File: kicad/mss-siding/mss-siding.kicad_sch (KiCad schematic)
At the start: 154 parts

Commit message: Add relay part number
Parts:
- K? (x3): value Panasonic_AGQ -> AGQ200A4H
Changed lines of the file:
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@@
     (in_bom yes) (on_board yes) (fields_autoplaced)
     (property "Reference" "K?" (id 0) (at 307.34 26.67 90))
-    (property "Value" "Panasonic_AGQ" (id 1) (at 307.34 29.21 90))
+    (property "Value" "AGQ200A4H" (id 1) (at 307.34 29.21 90))
     (property "Footprint" "Relay_THT:Relay_DPDT_Kemet_EC2" (id 2) (at 287.02 45.72 0)
       (effects (font (size 1.27 1.27)) hide)
@@
     (in_bom yes) (on_board yes) (fields_autoplaced)
     (property "Reference" "K?" (id 0) (at 319.405 96.52 90))
-    (property "Value" "Panasonic_AGQ" (id 1) (at 319.405 99.06 90))
+    (property "Value" "AGQ200A4H" (id 1) (at 319.405 99.06 90))
     (property "Footprint" "Relay_THT:Relay_DPDT_Kemet_EC2" (id 2) (at 299.085 115.57 0)
       (effects (font (size 1.27 1.27)) hide)
@@
   (symbol (lib_id "ISE_Generic:Panasonic_AGQ") (at 319.405 80.645 270) (mirror x) (unit 1)
     (in_bom yes) (on_board yes) (fields_autoplaced)
-    (property "Reference" "K?" (id 0) (at 319.405 61.595 90))
-    (property "Value" "Panasonic_AGQ" (id 1) (at 319.405 64.135 90))
+    (property "Reference" "K?" (id 0) (at 319.405 60.96 90))
+    (property "Value" "AGQ200A4H" (id 1) (at 319.405 63.5 90))
     (property "Footprint" "Relay_THT:Relay_DPDT_Kemet_EC2" (id 2) (at 299.085 80.645 0)
       (effects (font (size 1.27 1.27)) hide)
@@
     )
     (path "/29be23f3-d869-4d7a-be2a-612e20353779"
-      (reference "K?") (unit 1) (value "Panasonic_AGQ") (footprint "Relay_THT:Relay_DPDT_Kemet_EC2")
+      (reference "K?") (unit 1) (value "AGQ200A4H") (footprint "Relay_THT:Relay_DPDT_Kemet_EC2")
     )
     (path "/97b96930-9823-47ee-a628-f48c3e51fdb3"
-      (reference "K?") (unit 1) (value "Panasonic_AGQ") (footprint "Relay_THT:Relay_DPDT_Kemet_EC2")
+      (reference "K?") (unit 1) (value "AGQ200A4H") (footprint "Relay_THT:Relay_DPDT_Kemet_EC2")
     )
     (path "/c24a1838-bf5f-4b70-8cd9-fe7905500def"
-      (reference "K?") (unit 1) (value "Panasonic_AGQ") (footprint "Relay_THT:Relay_DPDT_Kemet_EC2")
+      (reference "K?") (unit 1) (value "AGQ200A4H") (footprint "Relay_THT:Relay_DPDT_Kemet_EC2")
     )
     (path "/1d1dcbdd-9d00-47cf-8c81-961826a4a57a"

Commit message: First cut of PCB
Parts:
- removed R? (x8): 10k, Resistor_SMD:R_0805_2012Metric, symbol Device:R_US
- added C20: 10uF, Capacitor_SMD:C_0805_2012Metric, symbol Device:C
- added R30, R31, R32, R33, R34, R35, R36, R38: 10k, Resistor_SMD:R_0805_2012Metric, symbol Device:R_US
- added unit 3 of U3
- added unit 2 of U3
- added unit 1 of U4
- added unit 2 of U4
- JP14, JP15, JP5: renamed from JP?; footprint (none) -> Jumper:SolderJumper-2_P1.3mm_Bridged_RoundedPad1.0x1.5mm
- K1, K2, K3: renamed from K?; footprint Relay_THT:Relay_DPDT_Kemet_EC2 -> ISE_UltraLibrarian:RELAY_AGQ_A_PAN
- gave numbers to parts that had none: 128
- renumbered H3 to H2, H2 to H3
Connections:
- net +12V: now also R25.2; no longer R25.1
- net +5V: now also J19.3 (Pin_3), C20.1; no longer J19.1 (Pin_1)
- net A_L_SIGNAL_G: now also J18.4 (MOSI), U6.1 (PB0); no longer U6.4 (PB3)
- net A_L_SIGNAL_R: now also U6.14 (PA4); no longer U6.12 (PA6), U6.17 (AREF/PA3)
- net A_L_SIGNAL_Y: now also U6.17 (AREF/PA3); no longer U6.11 (PA7), U6.14 (PA4)
- net A_U_SIGNAL_R: now also U6.11 (PA7)
- net A_U_SIGNAL_Y: now also U6.12 (PA6)
- net B_SIGNAL_G: now also U6.7 (XTAL1/PB4); no longer J18.4 (MOSI), U6.1 (PB0)
- net B_SIGNAL_R: now also U6.9 (PB6); no longer J18.3 (SCK), U6.3 (PB2)
- net B_SIGNAL_Y: now also U6.8 (XTAL2/PB5); no longer J18.1 (MISO), U6.2 (PB1)
- net COM_SENSE: now also U5.4 (IO0_0); no longer U5.13 (IO1_0)
- net C_SIGNAL_G: now also J18.1 (MISO), U6.2 (PB1); no longer U6.9 (PB6)
- net C_SIGNAL_R: now also U6.4 (PB3); no longer U6.7 (XTAL1/PB4)
- net C_SIGNAL_Y: now also J18.3 (SCK), U6.3 (PB2); no longer U6.8 (XTAL2/PB5)
- net FORCE_POINTS_AA: now also U5.10 (IO0_6); no longer U5.14 (IO1_1)
- net GND: now also C1.2, D4.2 (A), D5.2 (A), J19.1 (Pin_1), K3.3, C20.2, U3.5, U3.7, U4.3, U4.5; no longer J1.MP (MountPin), J11.MP (MountPin), J12.MP (MountPin), J19.3 (Pin_3), J2.MP (MountPin), K3.6
- net MAIN_AA_IN: now also R27.2, R35.1
- net MAIN_A_OUT: now also K3.4, K3.7; no longer K3.2, K3.5
- net POINTS_AA_IN: now also R26.2, R34.1
- net POINTS_AA_OUT: now also R24.2, R32.1
- net POINTS_A_IN: now also R25.1, R33.1
- net POINTS_A_OUT: now also R23.2, R31.1
- net POINTS_S: now also K3.6, R22.2, R30.1; no longer K3.3
- net RELAY_DRV: now also U5.11 (IO0_7); no longer U5.15 (IO1_2)
- net SIDE_AA_IN: now also R28.2, R36.1
- net SIDE_A_OUT: now also K3.2, K3.5; no longer K3.4, K3.7
- net TO_NORMAL: now also R29.2, R38.1
- net at J1.4 (Pin_4), J11.4 (Pin_4), J12.4 (Pin_4)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: now also J1.MP (MountPin), J11.MP (MountPin), J12.MP (MountPin), J2.MP (MountPin)
- net OPTION_D: now reaches U5.8 (IO0_4)
- net OPTION_D: now also JP19.2 (B); no longer U4.2
- net OPTION_B: now reaches U5.6 (IO0_2)
- net OPTION_B: now also JP17.2 (B); no longer U4.2
- net at U5.17 (IO1_4): now also U3.12; no longer JP19.2 (B)
- net at U5.16 (IO1_3): now also U3.10; no longer JP20.2 (B)
- net at U3.2: now also U5.19 (IO1_6); no longer U5.11 (IO0_7)
- net at C15.1, U3.3: now also R38.2; no longer R29.2
- net at U5.20 (IO1_7): now also U4.6; no longer JP16.2 (B)
- net at U5.18 (IO1_5): now also U3.15; no longer JP18.2 (B)
- net OPTION_E: now reaches U5.9 (IO0_5)
- net OPTION_E: now also JP20.2 (B); no longer U4.2
- net OPTION_A: now reaches U5.5 (IO0_1)
- net OPTION_A: now also JP16.2 (B); no longer U3.2
- net OPTION_C: now reaches U5.7 (IO0_3)
- net OPTION_C: now also JP18.2 (B); no longer U3.2
- new net: C14.1, R35.2, U4.7
- new net: C18.1, R34.2, U4.14
- new net: U4.15, U5.15 (IO1_2)
- new net: C16.1, R30.2, U3.14
- new net: C17.1, R32.2, U4.11
- new net: U4.12, U5.14 (IO1_1)
- new net: C19.1, R36.2, U4.9
- new net: C12.1, R31.2, U3.11
- new net: C13.1, R33.2, U3.9
- new net: U4.10, U5.13 (IO1_0)
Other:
- moved on the sheet: R21, R22, R23, R24, R25, R26, R27, R28, R29, TP18

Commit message: Fix a couple more booboos
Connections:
- net +5V: now also J19.1 (Pin_1); no longer J19.3 (Pin_3)
- net GND: now also J19.3 (Pin_3); no longer J19.1 (Pin_1)
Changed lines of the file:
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@@
     (pin "2")
   )
-  (symbol (lib_id "Connector:Screw_Terminal_01x03") (at 300.99 246.38 0) (mirror x) (unit 1)
+  (symbol (lib_id "Connector:Screw_Terminal_01x03") (at 300.99 246.38 0) (unit 1)
     (in_bom yes) (on_board yes)
-    (property "Reference" "J19" (id 0) (at 300.99 251.46 0))
-    (property "Value" "Screw_Terminal_01x02" (id 1) (at 300.99 250.19 0)
+    (property "Reference" "J19" (id 0) (at 300.99 241.3 0))
+    (property "Value" "Screw_Terminal_01x02" (id 1) (at 300.99 242.57 0)
       (effects (font (size 1.27 1.27)) hide)
     )

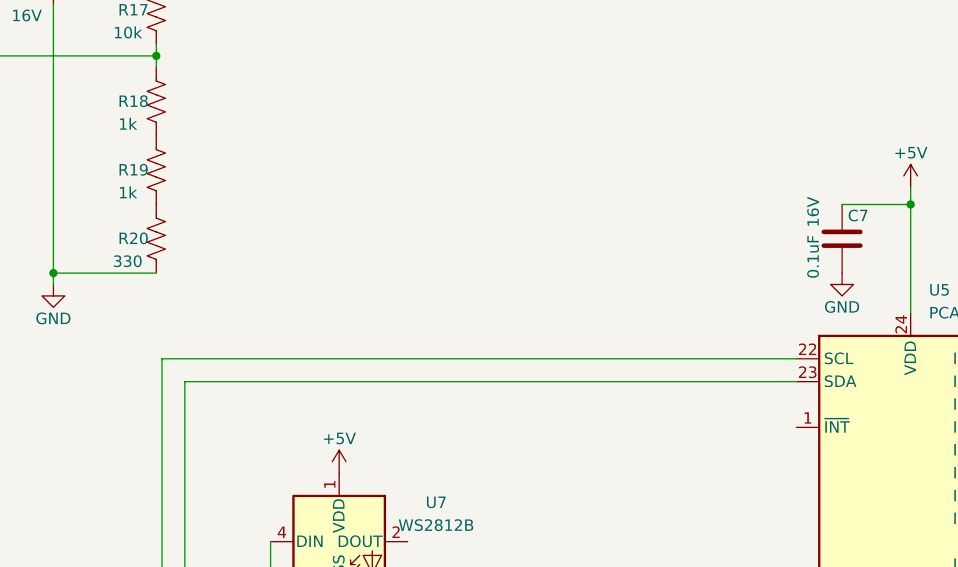
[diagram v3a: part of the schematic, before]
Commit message: Add I2C pull up resistors Fix some text issues
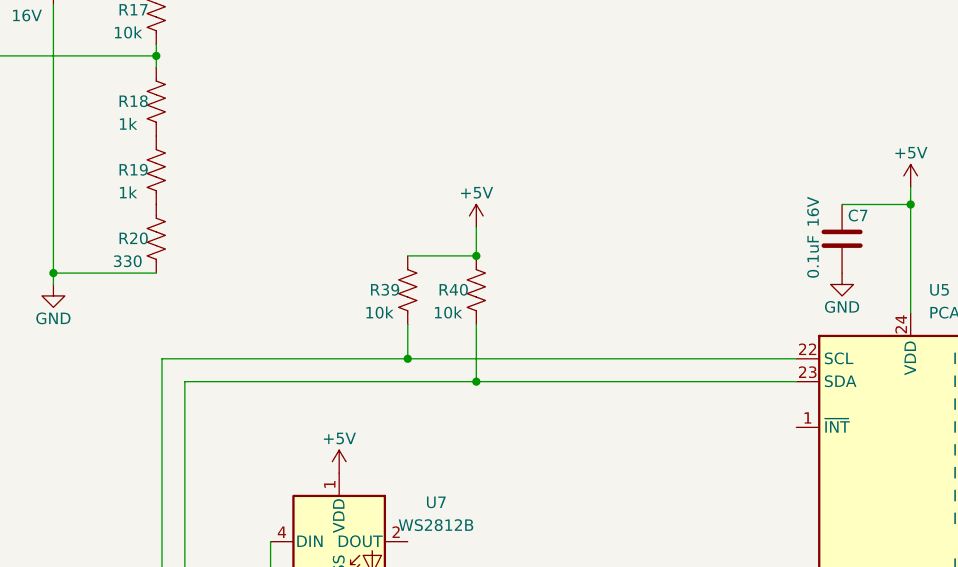
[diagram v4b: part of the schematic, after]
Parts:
- added R39, R40: 10k, Resistor_SMD:R_0805_2012Metric, symbol Device:R_US
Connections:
- net +5V: now also R39.2, R40.2
- net at U5.22 (SCL), U6.18 (PA2): now also R39.1
- net at U5.23 (SDA), U6.20 (PA0): now also R40.1
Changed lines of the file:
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@@
   (junction (at 139.7 94.615) (diameter 0) (color 0 0 0 0)
   )
+  (junction (at 108.585 162.56) (diameter 0) (color 0 0 0 0)
+  )
   (junction (at 336.55 222.885) (diameter 0) (color 0 0 0 0)
   )
@@
   (junction (at 229.235 94.615) (diameter 0) (color 0 0 0 0)
   )
+  (junction (at 116.205 165.1) (diameter 0) (color 0 0 0 0)
+  )
   (junction (at 368.3 31.115) (diameter 0) (color 0 0 0 0)
   )
@@
   (junction (at 161.925 64.135) (diameter 0) (color 0 0 0 0)
   )
+  (junction (at 116.205 151.13) (diameter 0) (color 0 0 0 0)
+  )
   (junction (at 259.715 146.05) (diameter 0) (color 0 0 0 0)
   )
@@
     (stroke (width 0) (type default) (color 0 0 0 0))
   )
+  (wire (pts (xy 108.585 151.13) (xy 116.205 151.13))
+    (stroke (width 0) (type default) (color 0 0 0 0))
+  )
   (wire (pts (xy 160.02 35.56) (xy 160.02 44.45))
     (stroke (width 0) (type default) (color 0 0 0 0))
@@
     (stroke (width 0) (type default) (color 0 0 0 0))
   )
+  (wire (pts (xy 116.205 147.955) (xy 116.205 151.13))
+    (stroke (width 0) (type default) (color 0 0 0 0))
+  )
   (wire (pts (xy 109.855 225.425) (xy 116.84 225.425))
     (stroke (width 0) (type default) (color 0 0 0 0))
@@
     (stroke (width 0) (type default) (color 0 0 0 0))
   )
+  (wire (pts (xy 116.205 165.1) (xy 83.82 165.1))
+    (stroke (width 0) (type default) (color 0 0 0 0))
+  )
   (wire (pts (xy 334.645 83.185) (xy 327.025 83.185))
     (stroke (width 0) (type default) (color 0 0 0 0))
@@
     (stroke (width 0) (type default) (color 0 0 0 0))
   )
+  (wire (pts (xy 116.205 158.75) (xy 116.205 165.1))
+    (stroke (width 0) (type default) (color 0 0 0 0))
+  )
   (wire (pts (xy 269.24 210.185) (xy 269.24 234.95))
     (stroke (width 0) (type default) (color 0 0 0 0))
@@
     (stroke (width 0) (type default) (color 0 0 0 0))
   )
-  (wire (pts (xy 151.765 165.1) (xy 83.82 165.1))
+  (wire (pts (xy 151.765 165.1) (xy 116.205 165.1))
     (stroke (width 0) (type default) (color 0 0 0 0))
   )
@@
     (stroke (width 0) (type default) (color 0 0 0 0))
   )
+  (wire (pts (xy 108.585 162.56) (xy 81.28 162.56))
+    (stroke (width 0) (type default) (color 0 0 0 0))
+  )
   (wire (pts (xy 69.215 153.035) (xy 69.215 154.305))
     (stroke (width 0) (type default) (color 0 0 0 0))
@@
     (stroke (width 0) (type default) (color 0 0 0 0))
   )
-  (wire (pts (xy 151.765 162.56) (xy 81.28 162.56))
+  (wire (pts (xy 151.765 162.56) (xy 108.585 162.56))
     (stroke (width 0) (type default) (color 0 0 0 0))
   )
@@
     (stroke (width 0) (type default) (color 0 0 0 0))
   )
+  (wire (pts (xy 108.585 158.75) (xy 108.585 162.56))
+    (stroke (width 0) (type default) (color 0 0 0 0))
+  )
   (wire (pts (xy 139.7 35.56) (xy 140.97 35.56))
     (stroke (width 0) (type default) (color 0 0 0 0))
@@
   (symbol (lib_id "power:GND") (at 109.22 257.81 0) (unit 1)
     (in_bom yes) (on_board yes)
-    (property "Reference" "#PWR?" (id 0) (at 109.22 264.16 0)
+    (property "Reference" "#PWR017" (id 0) (at 109.22 264.16 0)
       (effects (font (size 1.27 1.27)) hide)
     )
@@
     (pin "2")
   )
+  (symbol (lib_id "power:+5V") (at 116.205 147.955 0) (unit 1)
+    (in_bom yes) (on_board yes)
+    (property "Reference" "#PWR02" (id 0) (at 116.205 151.765 0)
+      (effects (font (size 1.27 1.27)) hide)
+    )
+    (property "Value" "+5V" (id 1) (at 116.205 144.145 0))
+    (property "Footprint" "" (id 2) (at 116.205 147.955 0)
+      (effects (font (size 1.27 1.27)) hide)
+    )
+    (property "Datasheet" "" (id 3) (at 116.205 147.955 0)
+      (effects (font (size 1.27 1.27)) hide)
+    )
+    (pin "1")
+  )
   (symbol (lib_id "Connector:TestPoint") (at 84.455 112.395 0) (mirror y) (unit 1)
     (in_bom yes) (on_board yes)
@@
   (symbol (lib_id "power:GND") (at 86.995 257.81 0) (unit 1)
     (in_bom yes) (on_board yes)
-    (property "Reference" "#PWR?" (id 0) (at 86.995 264.16 0)
+    (property "Reference" "#PWR03" (id 0) (at 86.995 264.16 0)
       (effects (font (size 1.27 1.27)) hide)
     )
@@
     (pin "1")
   )
+  (symbol (lib_id "Device:R_US") (at 108.585 154.94 180) (unit 1)
+    (in_bom yes) (on_board yes)
+    (property "Reference" "R39" (id 0) (at 106.045 154.94 0))
+    (property "Value" "10k" (id 1) (at 105.41 157.48 0))
+    (property "Footprint" "Resistor_SMD:R_0805_2012Metric" (id 2) (at 107.569 154.686 90)
+      (effects (font (size 1.27 1.27)) hide)
+    )
+    (property "Datasheet" "~" (id 3) (at 108.585 154.94 0)
+      (effects (font (size 1.27 1.27)) hide)
+    )
+    (pin "1")
+    (pin "2")
+  )
   (symbol (lib_id "Device:R_US") (at 269.875 200.66 270) (unit 1)
     (in_bom yes) (on_board yes)
@@
     (pin "1")
   )
+  (symbol (lib_id "Device:R_US") (at 116.205 154.94 180) (unit 1)
+    (in_bom yes) (on_board yes)
+    (property "Reference" "R40" (id 0) (at 113.665 154.94 0))
+    (property "Value" "10k" (id 1) (at 113.03 157.48 0))
+    (property "Footprint" "Resistor_SMD:R_0805_2012Metric" (id 2) (at 115.189 154.686 90)
+      (effects (font (size 1.27 1.27)) hide)
+    )
+    (property "Datasheet" "~" (id 3) (at 116.205 154.94 0)
+      (effects (font (size 1.27 1.27)) hide)
+    )
+    (pin "1")
+    (pin "2")
+  )
   (symbol (lib_id "Device:R_US") (at 144.78 35.56 90) (unit 1)
     (in_bom yes) (on_board yes)
@@
       (reference "#PWR01") (unit 1) (value "+12V") (footprint "")
     )
+    (path "/0cb219d0-a158-4c18-b8b7-9aaea6d986b8"
+      (reference "#PWR02") (unit 1) (value "+5V") (footprint "")
+    )
+    (path "/7a367fef-05b3-4cb2-86d5-1f0ca7375f3c"
+      (reference "#PWR03") (unit 1) (value "GND") (footprint "")
+    )
     (path "/aebad9ad-8911-4cf9-bde1-ce7c485df7c2"
       (reference "#PWR04") (unit 1) (value "GND") (footprint "")
@@
       (reference "#PWR016") (unit 1) (value "GND") (footprint "")
     )
+    (path "/03900267-0058-4b9e-9aaa-2c5ea2aebab7"
+      (reference "#PWR017") (unit 1) (value "GND") (footprint "")
+    )
     (path "/87e6f6e0-1bca-47ca-9ba8-9f4cd7552486"
       (reference "#PWR020") (unit 1) (value "+12V") (footprint "")
@@
       (reference "#PWR0103") (unit 1) (value "GND") (footprint "")
     )
-    (path "/03900267-0058-4b9e-9aaa-2c5ea2aebab7"
-      (reference "#PWR?") (unit 1) (value "GND") (footprint "")
-    )
-    (path "/7a367fef-05b3-4cb2-86d5-1f0ca7375f3c"
-      (reference "#PWR?") (unit 1) (value "GND") (footprint "")
-    )
     (path "/f7afeb96-08a7-44d0-9778-892656948ff0"
       (reference "C1") (unit 1) (value "68uF") (footprint "Capacitor_SMD:CP_Elec_6.3x5.8")
@@
       (reference "R38") (unit 1) (value "10k") (footprint "Resistor_SMD:R_0805_2012Metric")
     )
+    (path "/a90dd9ef-188b-443a-a735-8dd06eafe4f8"
+      (reference "R39") (unit 1) (value "10k") (footprint "Resistor_SMD:R_0805_2012Metric")
+    )
+    (path "/eaf07940-59df-4a54-85cb-117572f0b9aa"
+      (reference "R40") (unit 1) (value "10k") (footprint "Resistor_SMD:R_0805_2012Metric")
+    )
     (path "/a456ff59-9866-4634-a18c-c4c411e7d7e9"

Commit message: Design review improvements
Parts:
- added JP21: SolderJumper_2_Bridged, Jumper:SolderJumper-2_P1.3mm_Bridged_RoundedPad1.0x1.5mm, symbol Jumper:SolderJumper_2_Bridged
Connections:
- net TO_NORMAL: now also JP21.2 (B); no longer R29.2
- new net: JP21.1 (A), R29.2
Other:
- moved on the sheet: R29
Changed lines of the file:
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@@
   (junction (at 377.19 210.185) (diameter 0) (color 0 0 0 0)
   )
-  (junction (at 290.195 229.235) (diameter 0) (color 0 0 0 0)
-  )
   (junction (at 287.02 123.19) (diameter 0) (color 0 0 0 0)
   )
@@
   (junction (at 139.7 46.99) (diameter 0) (color 0 0 0 0)
   )
+  (junction (at 289.56 229.235) (diameter 0) (color 0 0 0 0)
+  )
   (junction (at 190.5 242.57) (diameter 0) (color 0 0 0 0)
   )
@@
     (stroke (width 0) (type default) (color 0 0 0 0))
   )
+  (wire (pts (xy 297.815 146.05) (xy 300.99 146.05))
+    (stroke (width 0) (type default) (color 0 0 0 0))
+  )
   (wire (pts (xy 160.655 85.09) (xy 163.195 85.09))
     (stroke (width 0) (type default) (color 0 0 0 0))
@@
     (stroke (width 0) (type default) (color 0 0 0 0))
   )
+  (wire (pts (xy 289.56 229.235) (xy 289.56 153.67))
+    (stroke (width 0) (type default) (color 0 0 0 0))
+  )
   (wire (pts (xy 69.215 123.19) (xy 69.215 153.035))
     (stroke (width 0) (type default) (color 0 0 0 0))
@@
     (stroke (width 0) (type default) (color 0 0 0 0))
   )
+  (wire (pts (xy 289.56 229.235) (xy 292.735 229.235))
+    (stroke (width 0) (type default) (color 0 0 0 0))
+  )
   (wire (pts (xy 368.3 31.115) (xy 368.3 33.655))
     (stroke (width 0) (type default) (color 0 0 0 0))
@@
     (stroke (width 0) (type default) (color 0 0 0 0))
   )
-  (wire (pts (xy 290.195 156.845) (xy 290.195 229.235))
-    (stroke (width 0) (type default) (color 0 0 0 0))
-  )
   (wire (pts (xy 156.21 20.32) (xy 156.21 46.99))
     (stroke (width 0) (type default) (color 0 0 0 0))
@@
     (stroke (width 0) (type default) (color 0 0 0 0))
   )
+  (wire (pts (xy 300.99 153.67) (xy 298.45 153.67))
+    (stroke (width 0) (type default) (color 0 0 0 0))
+  )
   (wire (pts (xy 151.765 198.12) (xy 151.765 200.66))
     (stroke (width 0) (type default) (color 0 0 0 0))
@@
     (stroke (width 0) (type default) (color 0 0 0 0))
   )
-  (wire (pts (xy 288.29 229.235) (xy 290.195 229.235))
+  (wire (pts (xy 288.29 229.235) (xy 289.56 229.235))
     (stroke (width 0) (type default) (color 0 0 0 0))
   )
@@
     (stroke (width 0) (type default) (color 0 0 0 0))
   )
-  (wire (pts (xy 290.195 229.235) (xy 292.735 229.235))
-    (stroke (width 0) (type default) (color 0 0 0 0))
-  )
   (wire (pts (xy 381.635 127) (xy 389.255 127))
     (stroke (width 0) (type default) (color 0 0 0 0))
@@
     (stroke (width 0) (type default) (color 0 0 0 0))
   )
-  (wire (pts (xy 290.195 146.05) (xy 290.195 149.225))
-    (stroke (width 0) (type default) (color 0 0 0 0))
-  )
   (wire (pts (xy 156.845 106.045) (xy 156.845 74.295))
     (stroke (width 0) (type default) (color 0 0 0 0))
@@
     (stroke (width 0) (type default) (color 0 0 0 0))
   )
+  (wire (pts (xy 300.99 146.05) (xy 300.99 153.67))
+    (stroke (width 0) (type default) (color 0 0 0 0))
+  )
   (wire (pts (xy 216.535 172.085) (xy 222.25 172.085))
     (stroke (width 0) (type default) (color 0 0 0 0))
@@
     (stroke (width 0) (type default) (color 0 0 0 0))
   )
+  (wire (pts (xy 289.56 153.67) (xy 290.83 153.67))
+    (stroke (width 0) (type default) (color 0 0 0 0))
+  )
   (wire (pts (xy 86.995 201.93) (xy 86.995 215.9))
     (stroke (width 0) (type default) (color 0 0 0 0))
@@
     (pin "2")
   )
+  (symbol (lib_id "Jumper:SolderJumper_2_Bridged") (at 294.64 153.67 180) (unit 1)
+    (in_bom yes) (on_board yes)
+    (property "Reference" "JP21" (id 0) (at 294.64 151.765 90)
+      (effects (font (size 1.27 1.27)) (justify right))
+    )
+    (property "Value" "SolderJumper_2_Bridged" (id 1) (at 294.64 157.48 0)
+      (effects (font (size 1.27 1.27)) hide)
+    )
+    (property "Footprint" "Jumper:SolderJumper-2_P1.3mm_Bridged_RoundedPad1.0x1.5mm" (id 2) (at 294.64 153.67 0)
+      (effects (font (size 1.27 1.27)) hide)
+    )
+    (property "Datasheet" "~" (id 3) (at 294.64 153.67 0)
+      (effects (font (size 1.27 1.27)) hide)
+    )
+    (pin "1")
+    (pin "2")
+  )
   (symbol (lib_id "Jumper:SolderJumper_2_Open") (at 224.155 53.34 0) (unit 1)
     (in_bom yes) (on_board yes)
@@
     (pin "2")
   )
-  (symbol (lib_id "Device:R_US") (at 290.195 153.035 0) (unit 1)
+  (symbol (lib_id "Device:R_US") (at 294.005 146.05 90) (unit 1)
     (in_bom yes) (on_board yes)
-    (property "Reference" "R29" (id 0) (at 292.735 154.94 90))
-    (property "Value" "10k" (id 1) (at 292.735 151.13 90))
-    (property "Footprint" "Resistor_SMD:R_0805_2012Metric" (id 2) (at 291.211 153.289 90)
+    (property "Reference" "R29" (id 0) (at 295.91 143.51 90))
+    (property "Value" "10k" (id 1) (at 292.1 143.51 90))
+    (property "Footprint" "Resistor_SMD:R_0805_2012Metric" (id 2) (at 294.259 145.034 90)
       (effects (font (size 1.27 1.27)) hide)
     )
-    (property "Datasheet" "~" (id 3) (at 290.195 153.035 0)
+    (property "Datasheet" "~" (id 3) (at 294.005 146.05 0)
       (effects (font (size 1.27 1.27)) hide)
     )
@@
       (reference "JP20") (unit 1) (value "SolderJumper_2_Open") (footprint "Jumper:SolderJumper-2_P1.3mm_Open_RoundedPad1.0x1.5mm")
     )
+    (path "/4580e792-e89f-4540-87ef-54eeb6757585"
+      (reference "JP21") (unit 1) (value "SolderJumper_2_Bridged") (footprint "Jumper:SolderJumper-2_P1.3mm_Bridged_RoundedPad1.0x1.5mm")
+    )
     (path "/29be23f3-d869-4d7a-be2a-612e20353779"
